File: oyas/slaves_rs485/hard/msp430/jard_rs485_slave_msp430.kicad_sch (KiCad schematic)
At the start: 60 parts, among them J1 POWER, J5 Prog MSP, U1 BPC_Alim3_3V, U1 MAX485E, U2 MSP430F1232IDW, Y1 8MHz

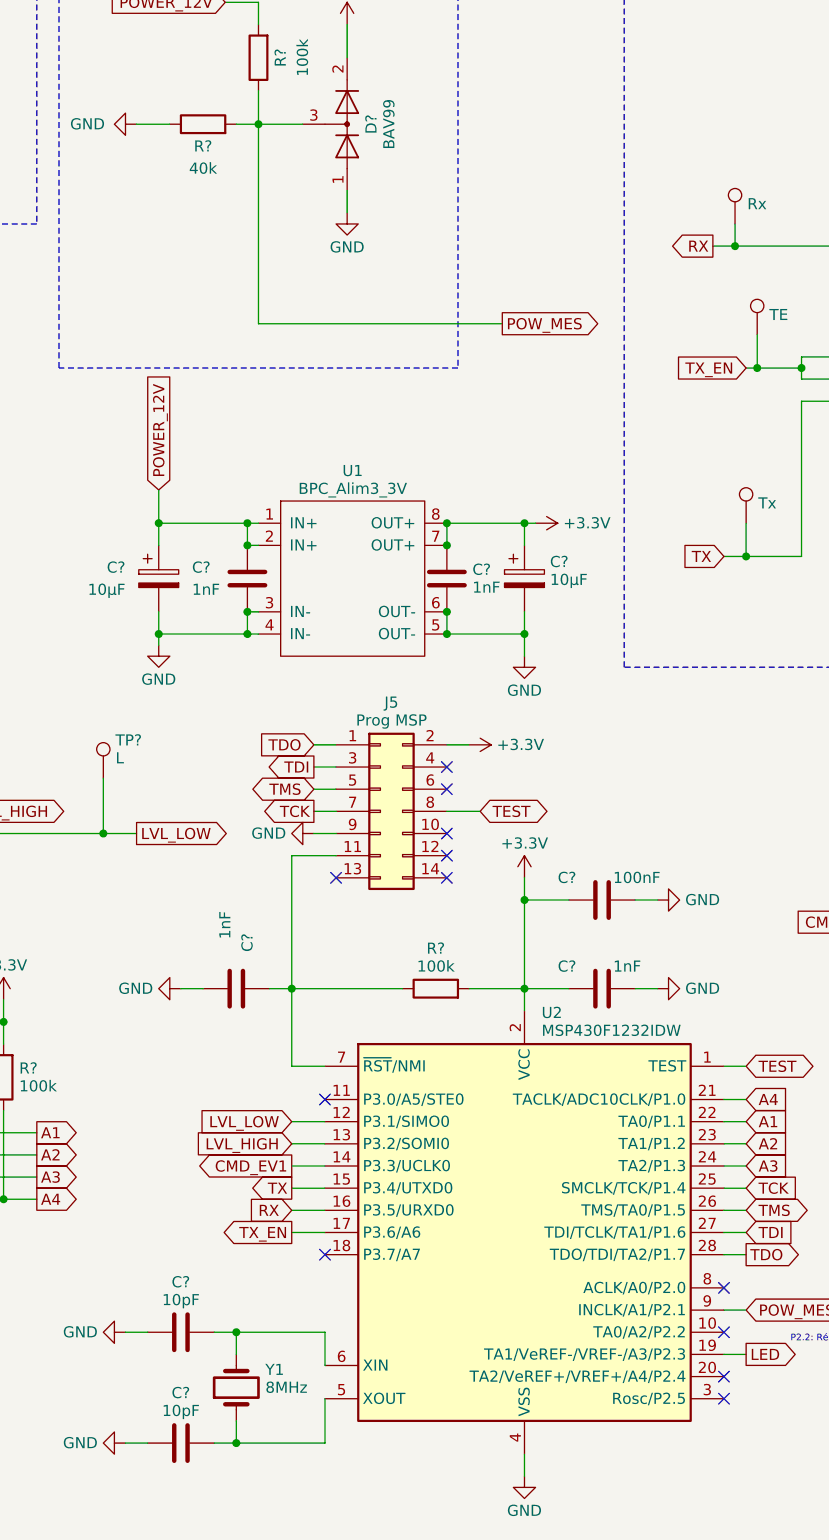
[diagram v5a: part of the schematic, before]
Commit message: Modification valeurs de composants - C10 100nF - R4 25k - C12 1µF
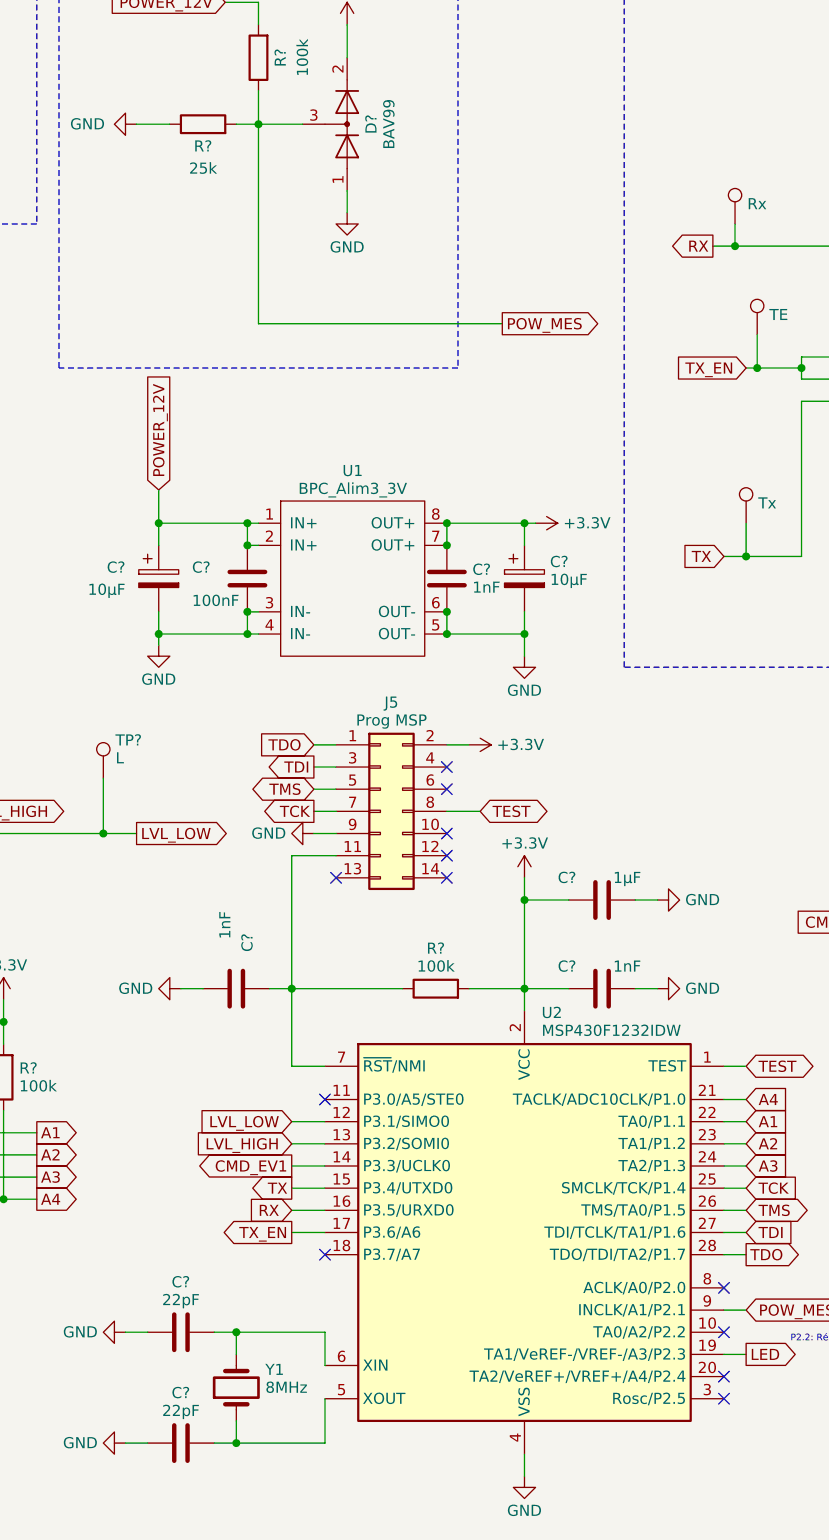
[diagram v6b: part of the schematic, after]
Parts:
- C?: value 100nF -> 1µF
- C? (x2): value 10pF -> 22pF
- C?: value 1nF -> 100nF
- R?: value 40k -> 25k
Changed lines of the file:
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@@
   (title_block
     (title "Esclave Oya MSP430")
-    (date "2025-04-13")
-    (rev "Rev B")
+    (date "2025-05-08")
+    (rev "Rev B1")
     (company "BPC")
     (comment 1 "Alim 12V - Bus RS485 - cmd EV/Pompe - Niveaux - Débit")
@@
       (effects (font (size 1.27 1.27)) (justify left))
     )
-    (property "Value" "100nF" (at 144.78 119.38 90)
+    (property "Value" "1µF" (at 144.78 119.38 90)
       (effects (font (size 1.27 1.27)) (justify left))
     )
@@
       (effects (font (size 1.27 1.27)))
     )
-    (property "Value" "10pF" (at 95.25 180.459 90)
+    (property "Value" "22pF" (at 95.25 180.459 90)
       (effects (font (size 1.27 1.27)))
     )
@@
       (effects (font (size 1.27 1.27)))
     )
-    (property "Value" "10pF" (at 95.25 167.759 90)
+    (property "Value" "22pF" (at 95.25 167.759 90)
       (effects (font (size 1.27 1.27)))
     )
@@
       (effects (font (size 1.27 1.27)) (justify left))
     )
-    (property "Value" "1nF" (at 96.52 86.36 0)
+    (property "Value" "100nF" (at 96.52 87.63 0)
       (effects (font (size 1.27 1.27)) (justify left))
     )
@@
       (effects (font (size 1.27 1.27)))
     )
-    (property "Value" "40k" (at 97.79 38.1 90)
+    (property "Value" "25k" (at 97.79 38.1 90)
       (effects (font (size 1.27 1.27)))
     )
